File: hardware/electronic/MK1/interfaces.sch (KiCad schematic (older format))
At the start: 4 parts, among them P1 CONN_01X08, P2 CONN_01X06, P3 CONN_01X10, P4 CONN_01X08

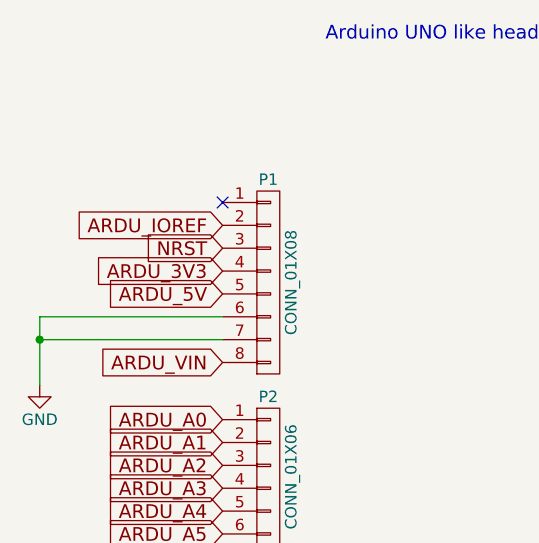
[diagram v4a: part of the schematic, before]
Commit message: HW: Start routing power traces
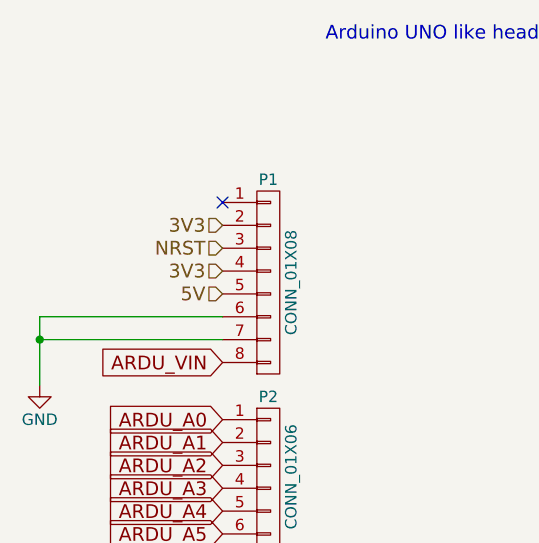
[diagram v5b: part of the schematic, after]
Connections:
- net ARDU_IOREF is gone; now on net 3V3: P1.2 (P2)
- net ARDU_3V3 renamed 3V3
- net ARDU_5V renamed 5V
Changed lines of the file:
@@
 Text GLabel 3550 3100 2    60   Input ~ 0
 ARDU_D0_RXD
-Text GLabel 1550 1750 0    60   Input ~ 0
-ARDU_IOREF
-Text GLabel 1550 1850 0    60   Input ~ 0
-NRST
-Text GLabel 1550 1950 0    60   Input ~ 0
-ARDU_3V3
-Text GLabel 1550 2050 0    60   Input ~ 0
-ARDU_5V
 Text GLabel 1550 2350 0    60   Input ~ 0
 ARDU_VIN
@@
 	1550 2250 750  2250
 Connection ~ 750  2250
+Text HLabel 1550 1950 0    60   Input ~ 0
+3V3
+Text HLabel 1550 2050 0    60   Input ~ 0
+5V
+Text HLabel 1550 1850 0    60   Input ~ 0
+NRST
+Text HLabel 1550 1750 0    60   Input ~ 0
+3V3
 $EndSCHEMATC

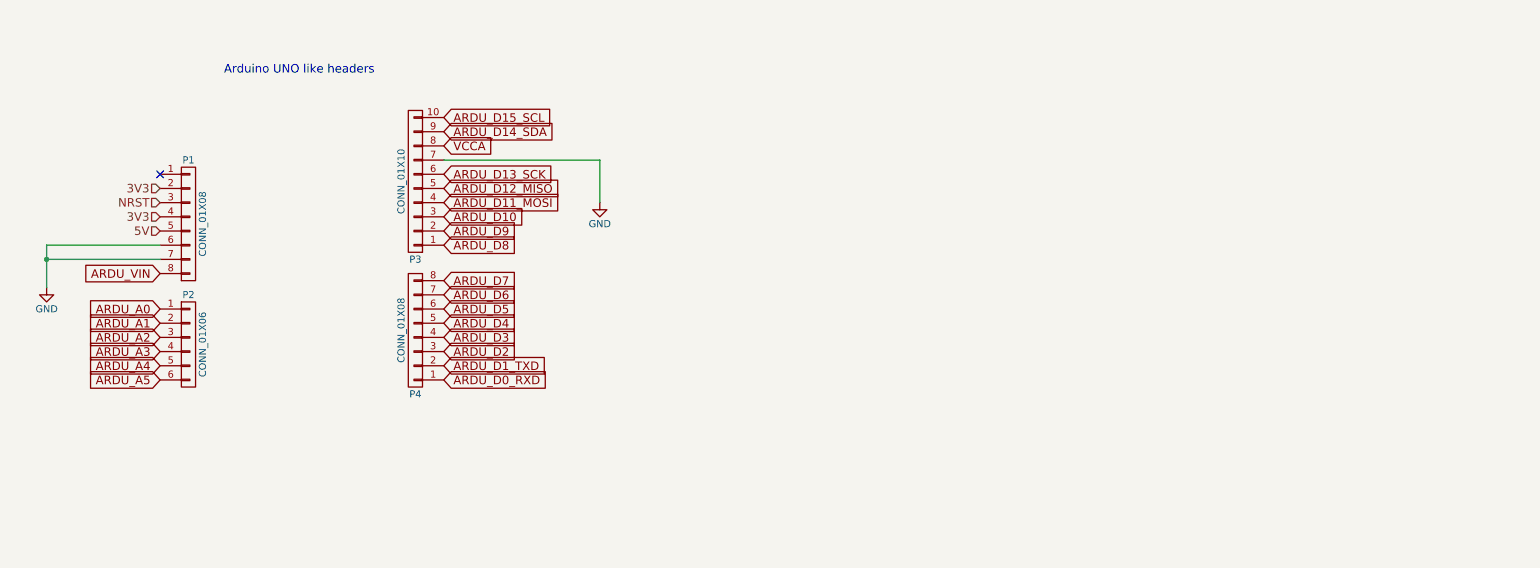
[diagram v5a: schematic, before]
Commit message: HW: Add BLE module
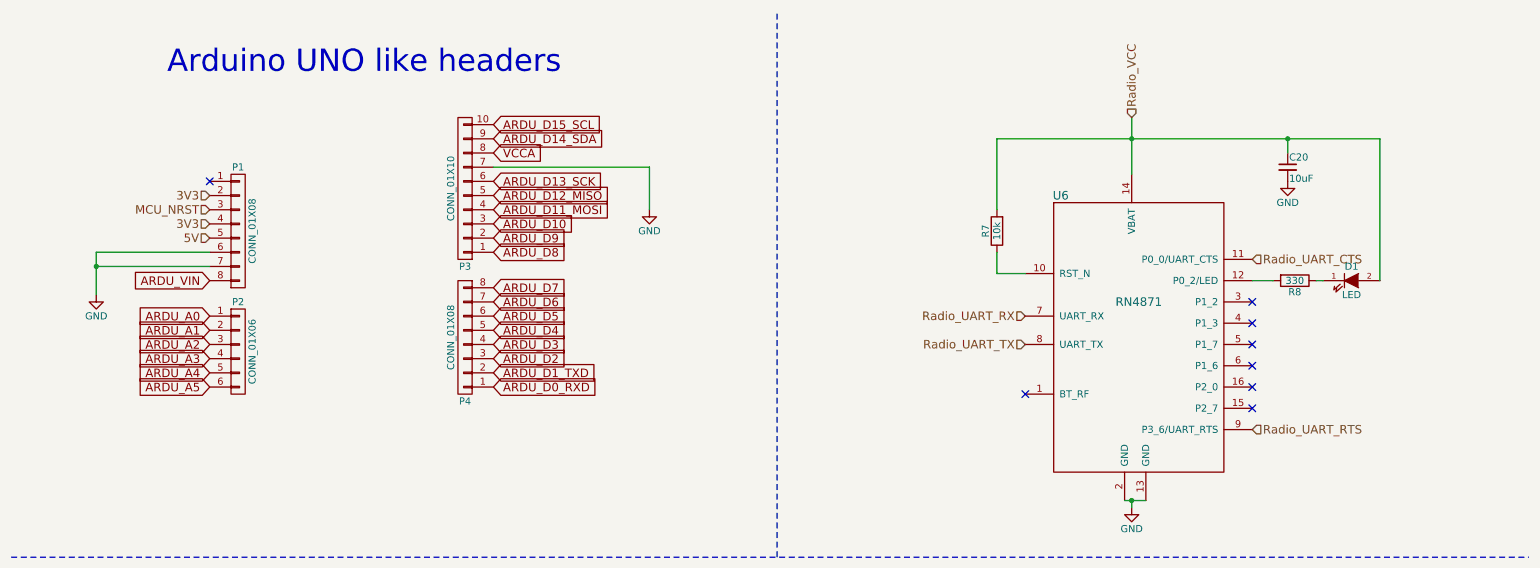
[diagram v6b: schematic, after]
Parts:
- added C20: 10uF, Capacitors_SMD:C_0805, symbol C_Small
- added D1: LED, LEDs:LED_0805, symbol LED
- added R7: 10k, Resistors_SMD:R_0805, symbol R
- added R8: 330, Resistors_SMD:R_0805, symbol R
- added U6: RN4871, OPAVES_Footprints:RN4871, symbol RN4871
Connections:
- net GND: now also C20.2, U6.13 (GND), U6.2 (GND)
- net NRST renamed MCU_NRST
- new net: R7.1, U6.10 (RST_N)
- new net: R8.2, U6.12 (P0_2/LED)
- new net: D1.1 (K), R8.1
- new net Radio_UART_CTS: U6.11 (P0_0/UART_CTS)
- new net Radio_UART_RTS: U6.9 (P3_6/UART_RTS)
- new net Radio_UART_RX: U6.7 (UART_RX)
- new net Radio_UART_TX: U6.8 (UART_TX)
- new net Radio_VCC: C20.1, D1.2 (A), R7.2, U6.14 (VBAT)
- no-connect marks 1 -> 8
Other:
- moved on the sheet: P1, P2, P3, P4

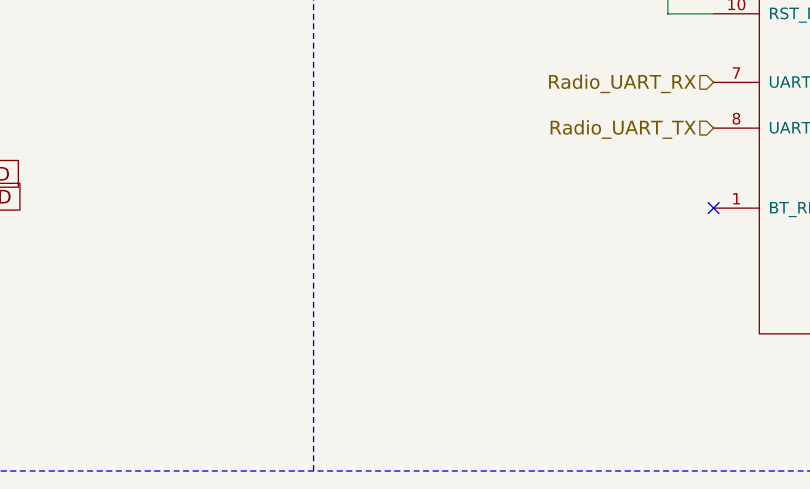
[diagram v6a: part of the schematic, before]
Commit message: HW: Start signal assignment and routing
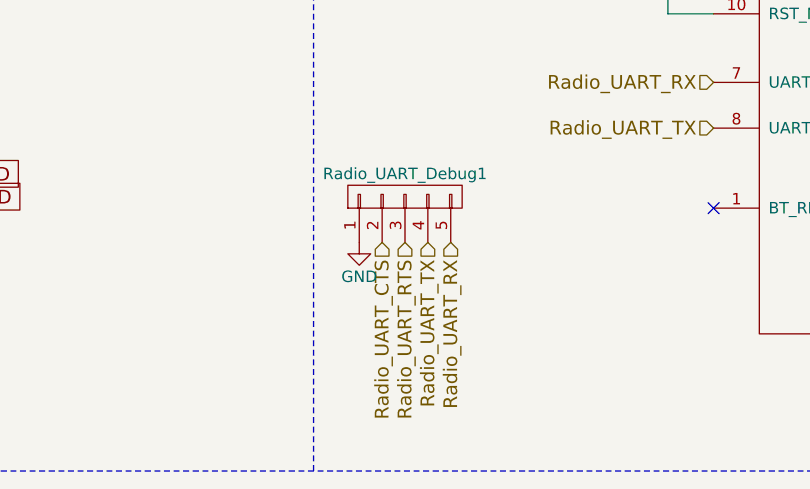
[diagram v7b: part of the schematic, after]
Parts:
- added Radio_UART_Debug1: Radio_UART, Pin_Headers:Pin_Header_Straight_1x05, symbol CONN_01X05
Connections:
- net GND: now also Radio_UART_Debug1.1 (P1)
- net Radio_UART_CTS: now also Radio_UART_Debug1.2 (P2)
- net Radio_UART_RTS: now also Radio_UART_Debug1.3 (P3)
- net Radio_UART_RX: now also Radio_UART_Debug1.5 (P5)
- net Radio_UART_TX: now also Radio_UART_Debug1.4 (P4)
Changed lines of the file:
@@
 ARDU_A5
 $Comp
-L GND #PWR017
+L GND #PWR17
 U 1 1 5886770A
 P 1100 2500
-F 0 "#PWR017" H 1100 2250 50  0001 C CNN
+F 0 "#PWR17" H 1100 2250 50  0001 C CNN
 F 1 "GND" H 1100 2350 50  0000 C CNN
 F 2 "" H 1100 2500 50  0000 C CNN
@@
 NoConn ~ 1900 1700
 $Comp
-L GND #PWR018
+L GND #PWR18
 U 1 1 5886A835
 P 5000 1900
-F 0 "#PWR018" H 5000 1650 50  0001 C CNN
+F 0 "#PWR18" H 5000 1650 50  0001 C CNN
 F 1 "GND" H 5000 1750 50  0000 C CNN
 F 2 "" H 5000 1900 50  0000 C CNN
@@
 Radio_VCC
 $Comp
-L GND #PWR019
+L GND #PWR20
 U 1 1 5890972B
 P 8400 4000
-F 0 "#PWR019" H 8400 3750 50  0001 C CNN
+F 0 "#PWR20" H 8400 3750 50  0001 C CNN
 F 1 "GND" H 8400 3850 50  0000 C CNN
 F 2 "" H 8400 4000 50  0000 C CNN
@@
 	8400 1250 8400 1650
 $Comp
-L GND #PWR020
+L GND #PWR21
 U 1 1 58909C4C
 P 9500 1700
-F 0 "#PWR020" H 9500 1450 50  0001 C CNN
+F 0 "#PWR21" H 9500 1450 50  0001 C CNN
 F 1 "GND" H 9500 1550 50  0000 C CNN
 F 2 "" H 9500 1700 50  0000 C CNN
@@
 	9500 1500 9500 1400
 Connection ~ 9500 1400
+Text HLabel 6300 3350 3    60   Input ~ 0
+Radio_UART_RTS
+Text HLabel 6200 3350 3    60   Input ~ 0
+Radio_UART_CTS
+Text HLabel 6500 3350 3    60   Input ~ 0
+Radio_UART_RX
+Text HLabel 6400 3350 3    60   Input ~ 0
+Radio_UART_TX
+$Comp
+L CONN_01X05 Radio_UART_Debug1
+U 1 1 58936C45
+P 6300 3150
+F 0 "Radio_UART_Debug1" V 6400 3150 50  0000 C CNN
+F 1 "Radio_UART" V 6400 3150 50  0001 C CNN
+F 2 "Pin_Headers:Pin_Header_Straight_1x05" H 6300 3150 50  0001 C CNN
+F 3 "" H 6300 3150 50  0000 C CNN
+	1    6300 3150
+	0    -1   -1   0
+$EndComp
+$Comp
+L GND #PWR19
+U 1 1 58936DB2
+P 6100 3350
+F 0 "#PWR19" H 6100 3100 50  0001 C CNN
+F 1 "GND" H 6100 3200 50  0000 C CNN
+F 2 "" H 6100 3350 50  0000 C CNN
+F 3 "" H 6100 3350 50  0000 C CNN
+	1    6100 3350
+	1    0    0    -1
+$EndComp
 $EndSCHEMATC

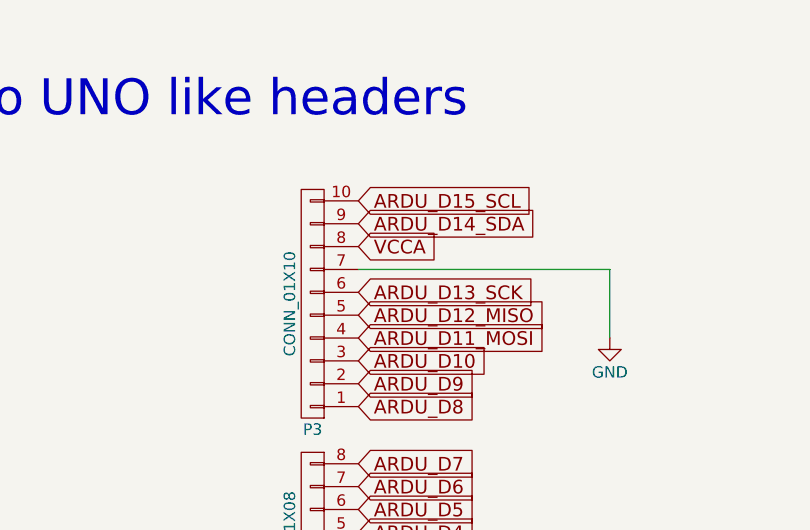
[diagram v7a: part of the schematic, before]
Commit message: HW: Signal assignment and routing cont.
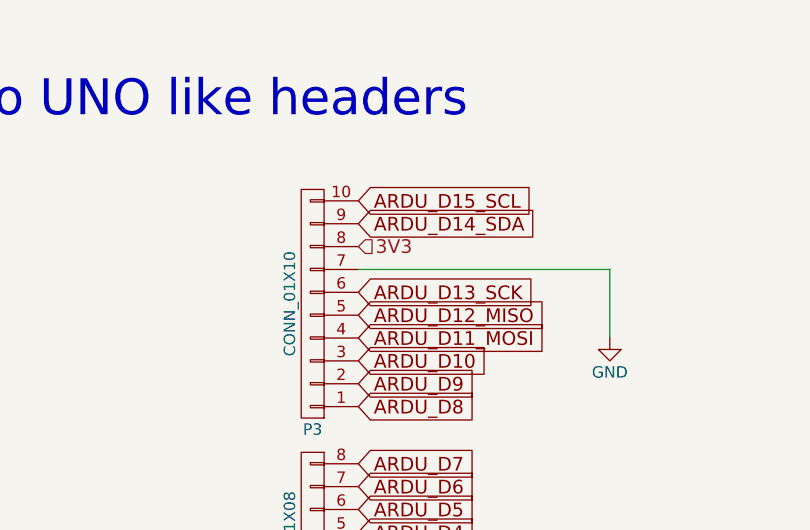
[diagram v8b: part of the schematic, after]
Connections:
- net VCCA is gone; now on net 3V3: P3.8 (P8)
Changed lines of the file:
@@
 Text GLabel 3900 1400 2    60   Input ~ 0
 ARDU_D14_SDA
-Text GLabel 3900 1500 2    60   Input ~ 0
-VCCA
 Text GLabel 3900 1700 2    60   Input ~ 0
 ARDU_D13_SCK
@@
 ARDU_A5
 $Comp
-L GND #PWR17
+L GND #PWR018
 U 1 1 5886770A
 P 1100 2500
-F 0 "#PWR17" H 1100 2250 50  0001 C CNN
+F 0 "#PWR018" H 1100 2250 50  0001 C CNN
 F 1 "GND" H 1100 2350 50  0000 C CNN
 F 2 "" H 1100 2500 50  0000 C CNN
@@
 NoConn ~ 1900 1700
 $Comp
-L GND #PWR18
+L GND #PWR019
 U 1 1 5886A835
 P 5000 1900
-F 0 "#PWR18" H 5000 1650 50  0001 C CNN
+F 0 "#PWR019" H 5000 1650 50  0001 C CNN
 F 1 "GND" H 5000 1750 50  0000 C CNN
 F 2 "" H 5000 1900 50  0000 C CNN
@@
 Radio_VCC
 $Comp
-L GND #PWR20
+L GND #PWR020
 U 1 1 5890972B
 P 8400 4000
-F 0 "#PWR20" H 8400 3750 50  0001 C CNN
+F 0 "#PWR020" H 8400 3750 50  0001 C CNN
 F 1 "GND" H 8400 3850 50  0000 C CNN
 F 2 "" H 8400 4000 50  0000 C CNN
@@
 	8400 1250 8400 1650
 $Comp
-L GND #PWR21
+L GND #PWR021
 U 1 1 58909C4C
 P 9500 1700
-F 0 "#PWR21" H 9500 1450 50  0001 C CNN
+F 0 "#PWR021" H 9500 1450 50  0001 C CNN
 F 1 "GND" H 9500 1550 50  0000 C CNN
 F 2 "" H 9500 1700 50  0000 C CNN
@@
 $EndComp
 $Comp
-L GND #PWR19
+L GND #PWR022
 U 1 1 58936DB2
 P 6100 3350
-F 0 "#PWR19" H 6100 3100 50  0001 C CNN
+F 0 "#PWR022" H 6100 3100 50  0001 C CNN
 F 1 "GND" H 6100 3200 50  0000 C CNN
 F 2 "" H 6100 3350 50  0000 C CNN
@@
 	1    0    0    -1
 $EndComp
+Text HLabel 3900 1500 2    60   Input ~ 0
+3V3
 $EndSCHEMATC
